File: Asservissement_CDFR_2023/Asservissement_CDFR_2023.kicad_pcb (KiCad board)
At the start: 2 copper layers, 87 x 115 mm, 161 parts, among them IC1 A3930KJPTR-T, IC2 A3930KJPTR-T, J1 Connecteur batterie, J10 Free Connecteur, J11 Conn_01x02, J12 Conn_01x02, J13 Connecteur Odométrie, J2 Conn_01x03, J3 Conn_01x05, J4 Connecteur Programmation, J5 Conn_01x03, J6 Connecteur Odométrie, J7 Conn_01x03, J8 Conn_01x03, J9 Conn_01x05, Q1 QM6006D, Q10 QM6006D, Q11 QM6006D, Q12 QM6006D, Q13 Q_NMOS_GDS, Q2 QM6006D, Q3 QM6006D, Q4 QM6006D, Q5 QM6006D, Q6 QM6006D, Q7 QM6006D, Q8 QM6006D, Q9 QM6006D, U1 LM317_SOT-223, U3 STM32F401RCTx, U4 LMR16020PDDA, Y1 Crystal_GND24

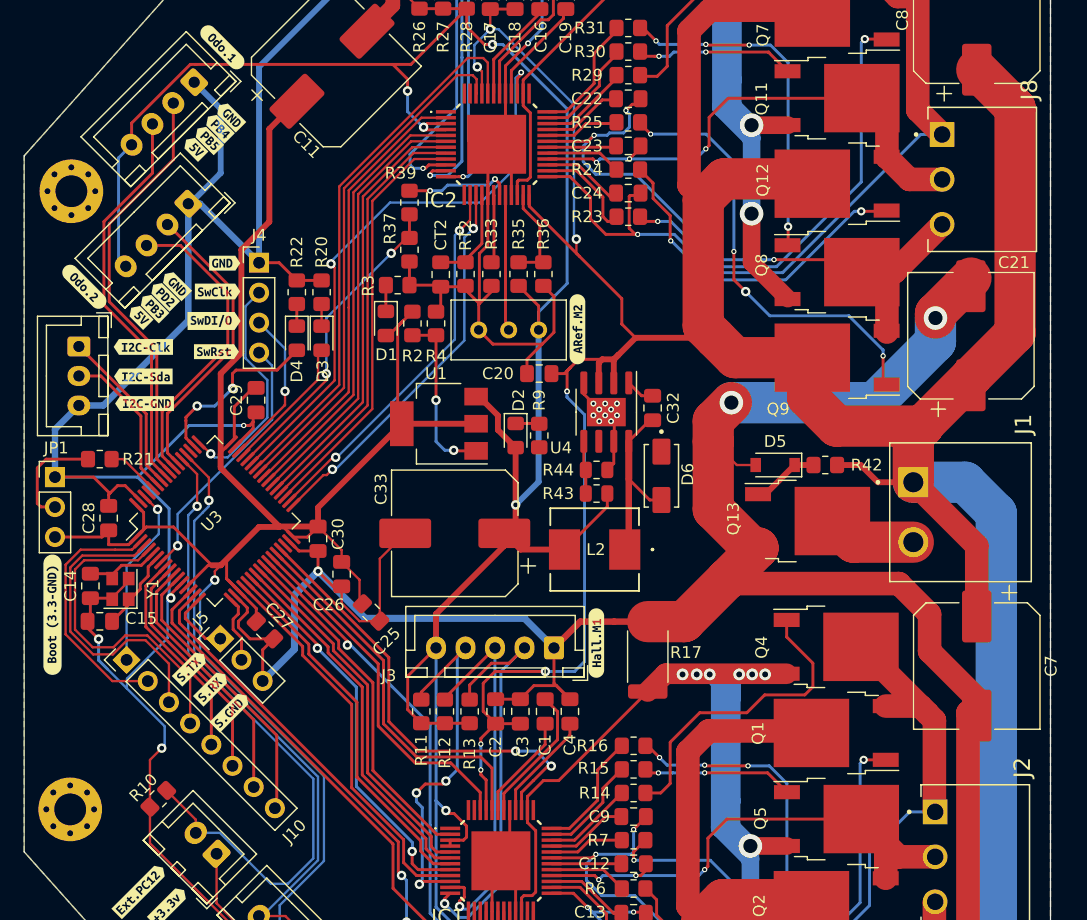
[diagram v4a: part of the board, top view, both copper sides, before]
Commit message: add resistor for the crystal, add capacitor to Vcap, add logo and text for the voltage tolerance
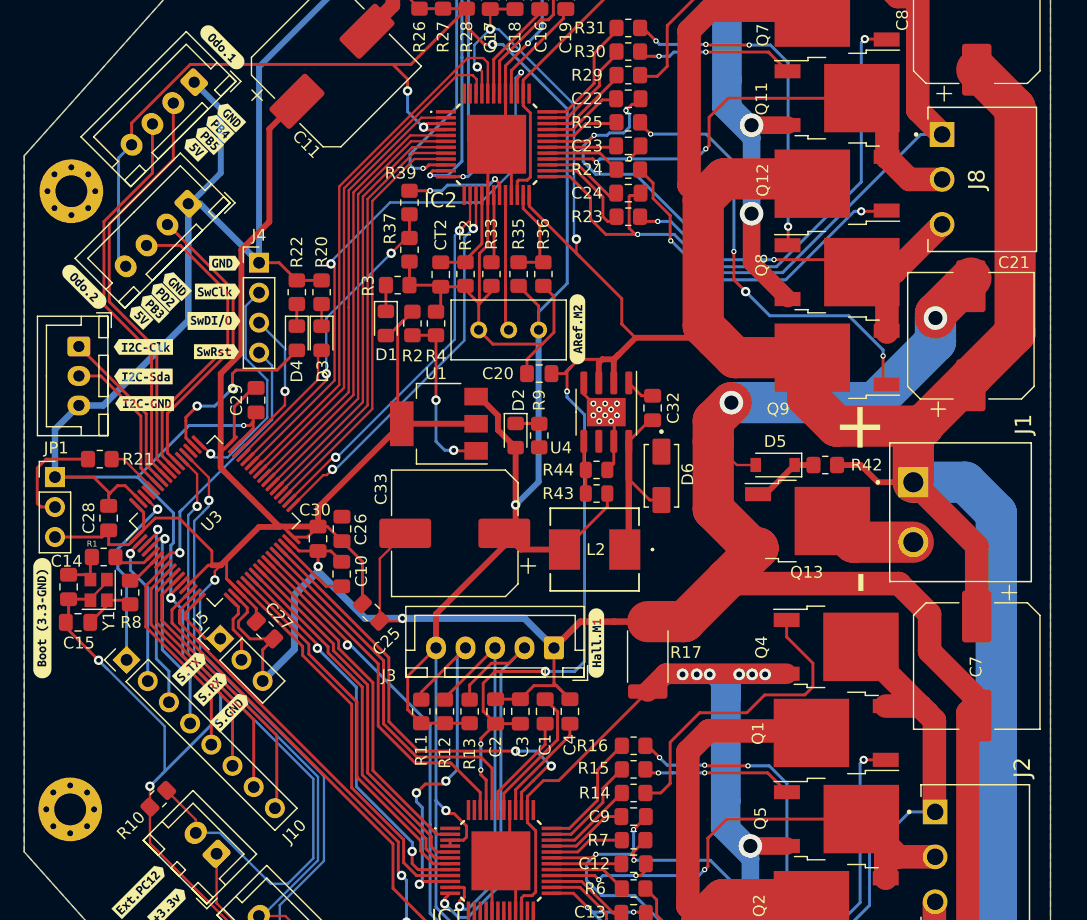
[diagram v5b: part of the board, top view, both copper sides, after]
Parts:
- added C10: 4.7uF, Capacitor_SMD:C_0805_2012Metric_Pad1.18x1.45mm_HandSolder, F.Cu at (61.5, 93.0)
- added G***: LOGO, logo:robotronik, B.Cu at (73.1, 87.1)
- added R1: 10k, Resistor_SMD:R_0805_2012Metric_Pad1.20x1.40mm_HandSolder, F.Cu at (41.3, 91.6)
- added R8: 10k, Resistor_SMD:R_0805_2012Metric_Pad1.20x1.40mm_HandSolder, F.Cu at (43.6, 94.6)
- moved C26 3.84 mm to (61.5, 89.2), turned to 90 degrees
- moved C14 1.85 mm to (38.4, 94.1)
- moved C15 1.85 mm to (39.2, 97.1)
- moved Y1 1.85 mm to (40.9, 94.3)
- moved kibuzzard-637D428D 0.91 mm to (36.1, 96.7)
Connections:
- U3 pad 30: unconnected-(U3-Pad30) -> Net-(U3-Pad30)
- U3 pad 5: Net-(C14-Pad2) -> Net-(U3-Pad5)
- U3 pad 6: Net-(C15-Pad1) -> Net-(U3-Pad6)
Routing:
- net Free4: track 28.2 -> 18.5 mm, vias 0 -> 1
- net Free3: track 26.3 -> 17.0 mm, vias 0 -> 1
- net Free2: track 21.7 -> 12.8 mm, vias 0 -> 1
- net GND: track 584.5 -> 591.2 mm, vias 19 -> 20
- net Net-(U3-Pad30): track 0.00 -> 6.23 mm
- net Net-(U3-Pad5): track 0.00 -> 3.69 mm
- net Net-(U3-Pad6): track 0.00 -> 3.08 mm
- net Net-(C14-Pad2): track 6.53 -> 3.98 mm
- net Net-(C15-Pad1): track 7.02 -> 4.57 mm
- net +3.3V: track 181.0 -> 182.7 mm
- net Free1: track 15.5 -> 16.0 mm
- net Net-(J4-Pad4): track 22.1 -> 22.6 mm
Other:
- board text added: "+"
- board text added: "-"
- board text added: "6V - 50V"

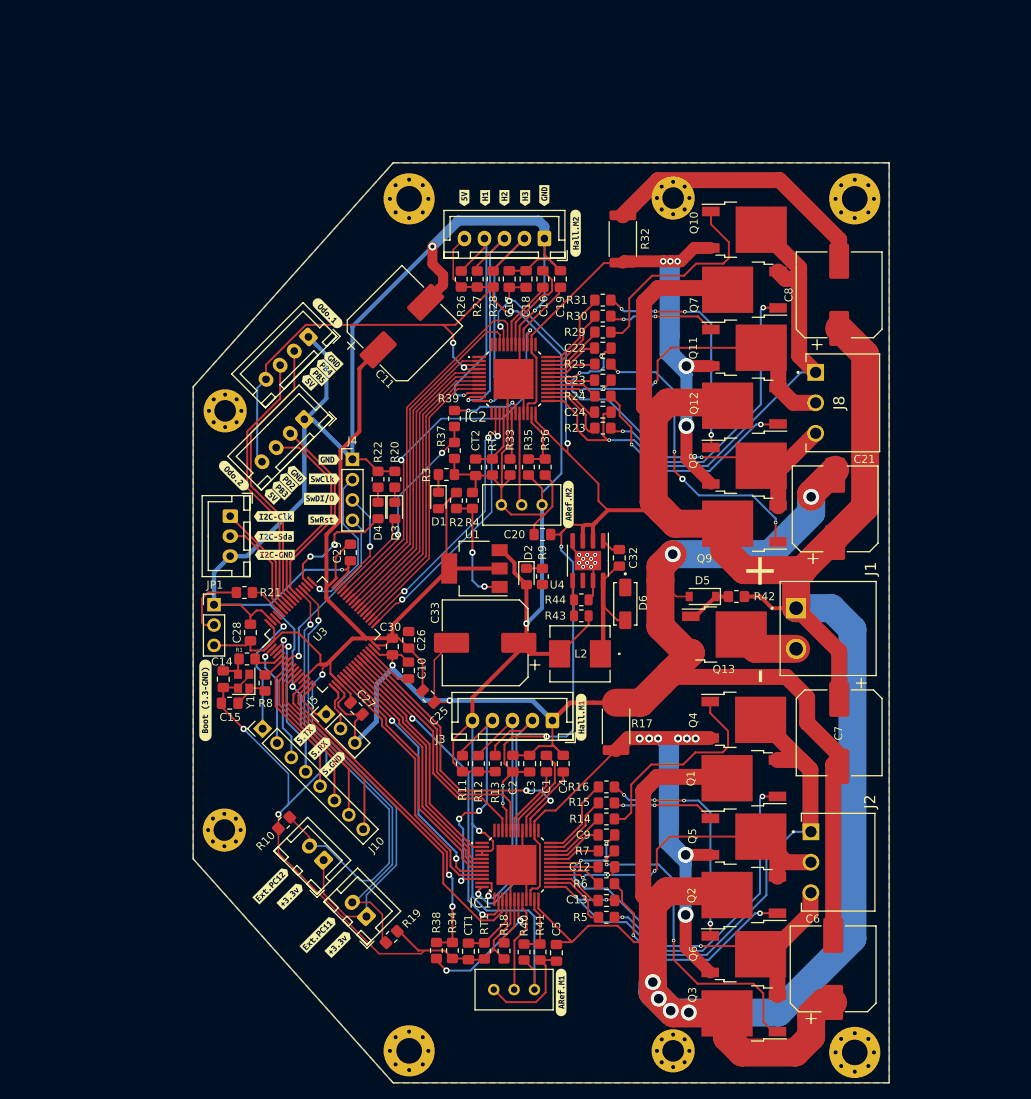
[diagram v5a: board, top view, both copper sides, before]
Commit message: add name and version
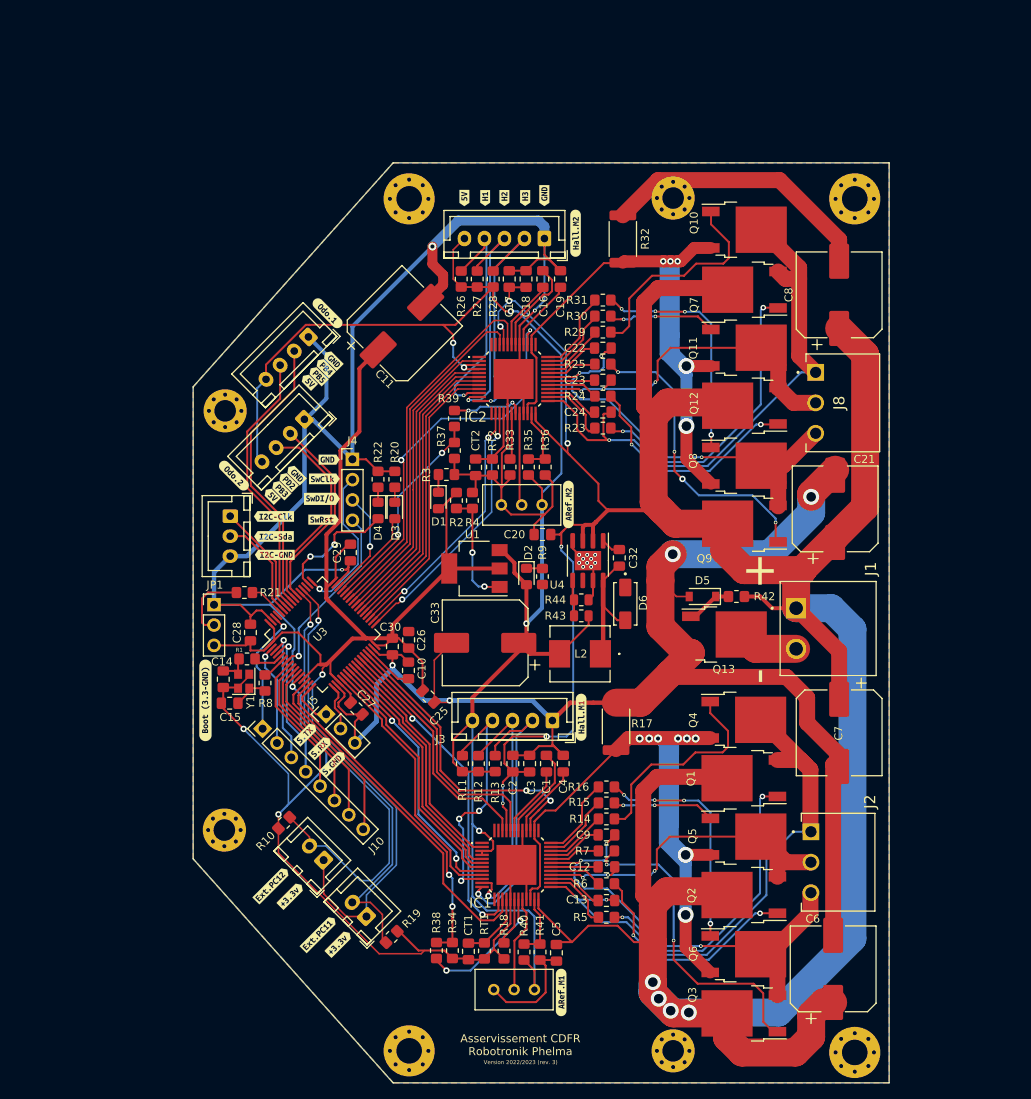
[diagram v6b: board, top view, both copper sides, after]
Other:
- board text added: "Asservissement CDFR Robotronik Phelma"
- board text added: "Version 2022/2023 (rev. 3)"

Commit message: add jlcjlcjlc
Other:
- board text added: "JLCJLCJLCJLC"
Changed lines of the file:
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@@
     (effects (font (size 2 2) (thickness 0.5)) (justify mirror))
+  )
+  (gr_text "JLCJLCJLCJLC" (at 71.3678 89.5518 90) (layer "F.SilkS")
+    (effects (font (size 0.2 0.2) (thickness 0.0375)))
   )
   (gr_text "Version 2022/2023 (rev. 3)" (at 75.5334 141.9774) (layer "F.SilkS")
